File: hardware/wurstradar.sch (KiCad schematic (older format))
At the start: 11 parts

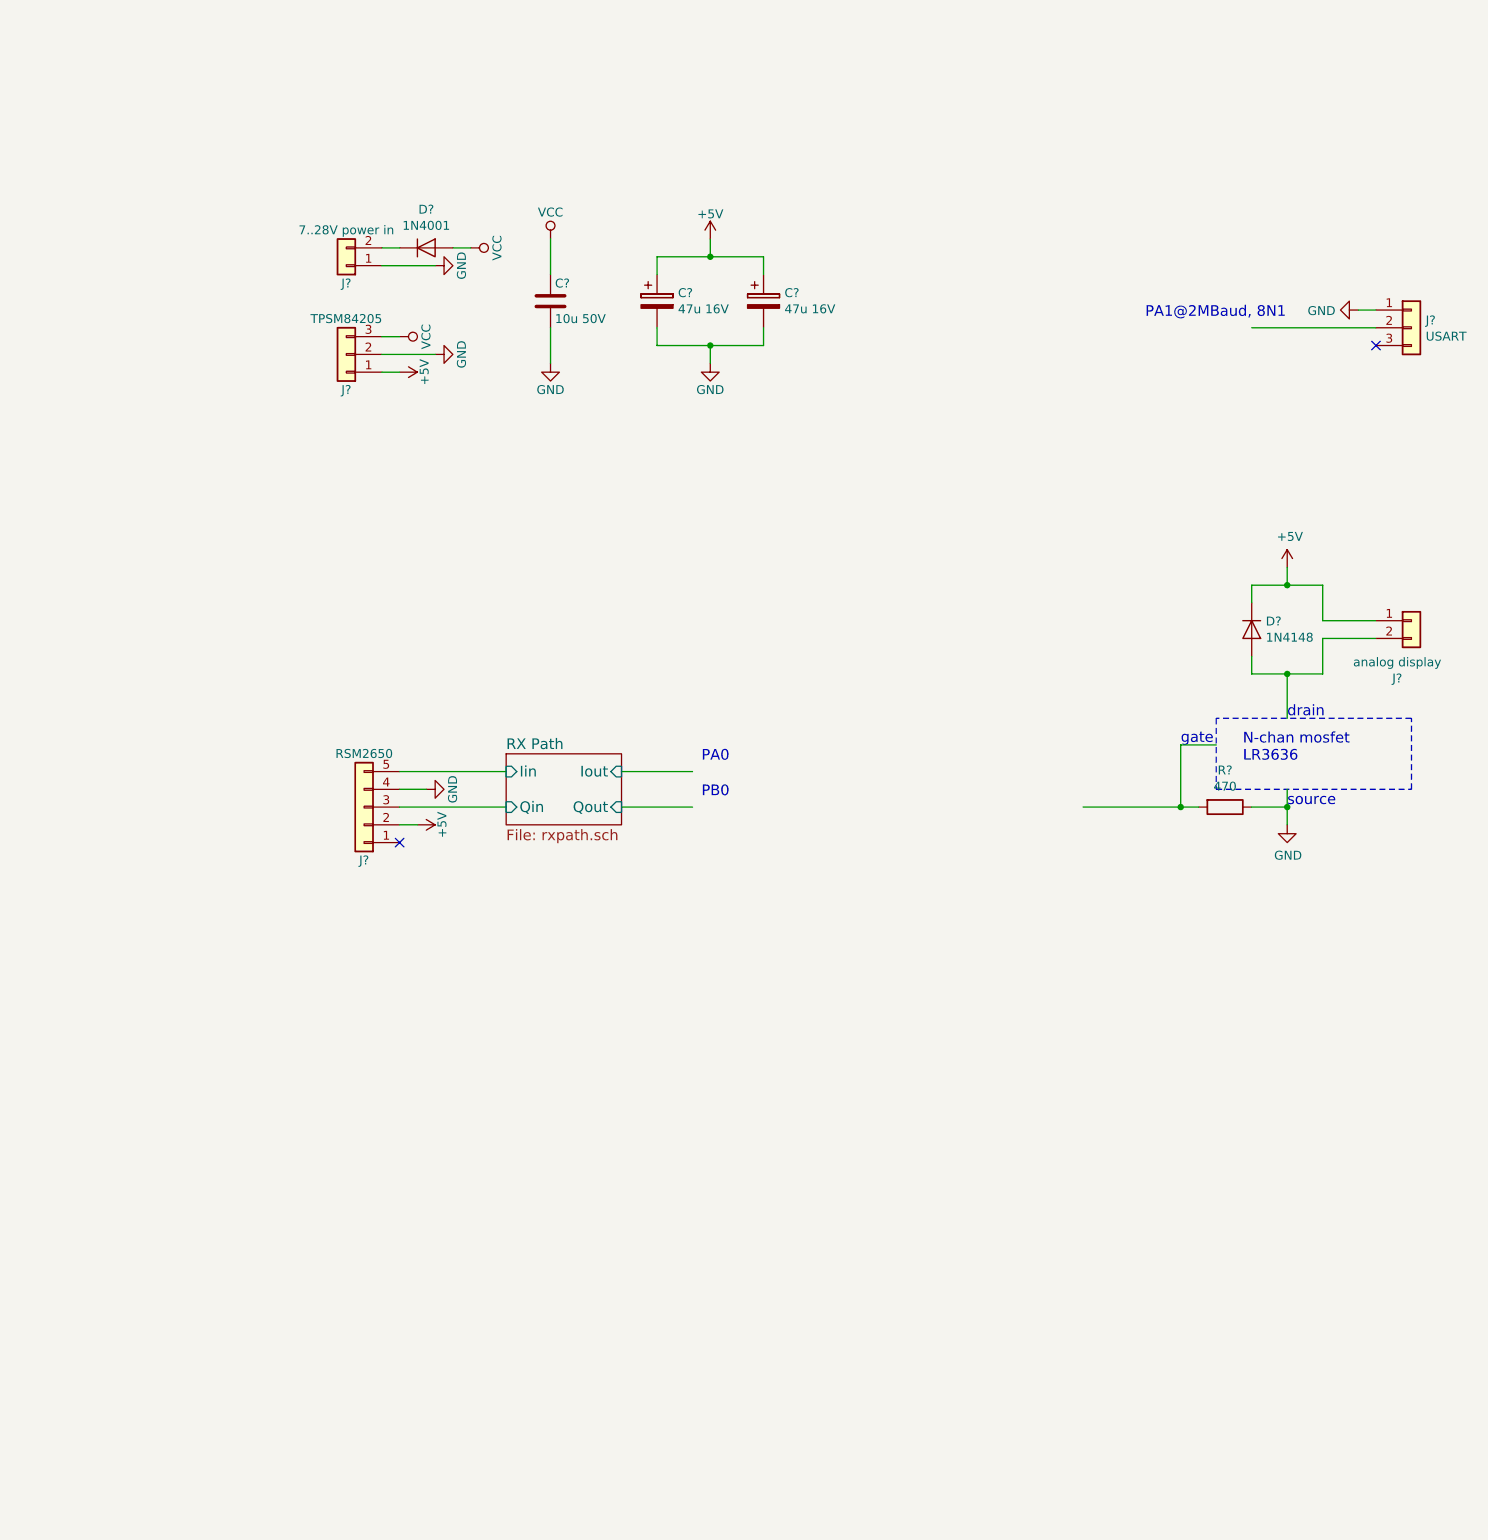
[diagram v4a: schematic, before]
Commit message: for long-term documentation: cleanup and port schematic to Kicad v5.1.4 and also export as PDF.
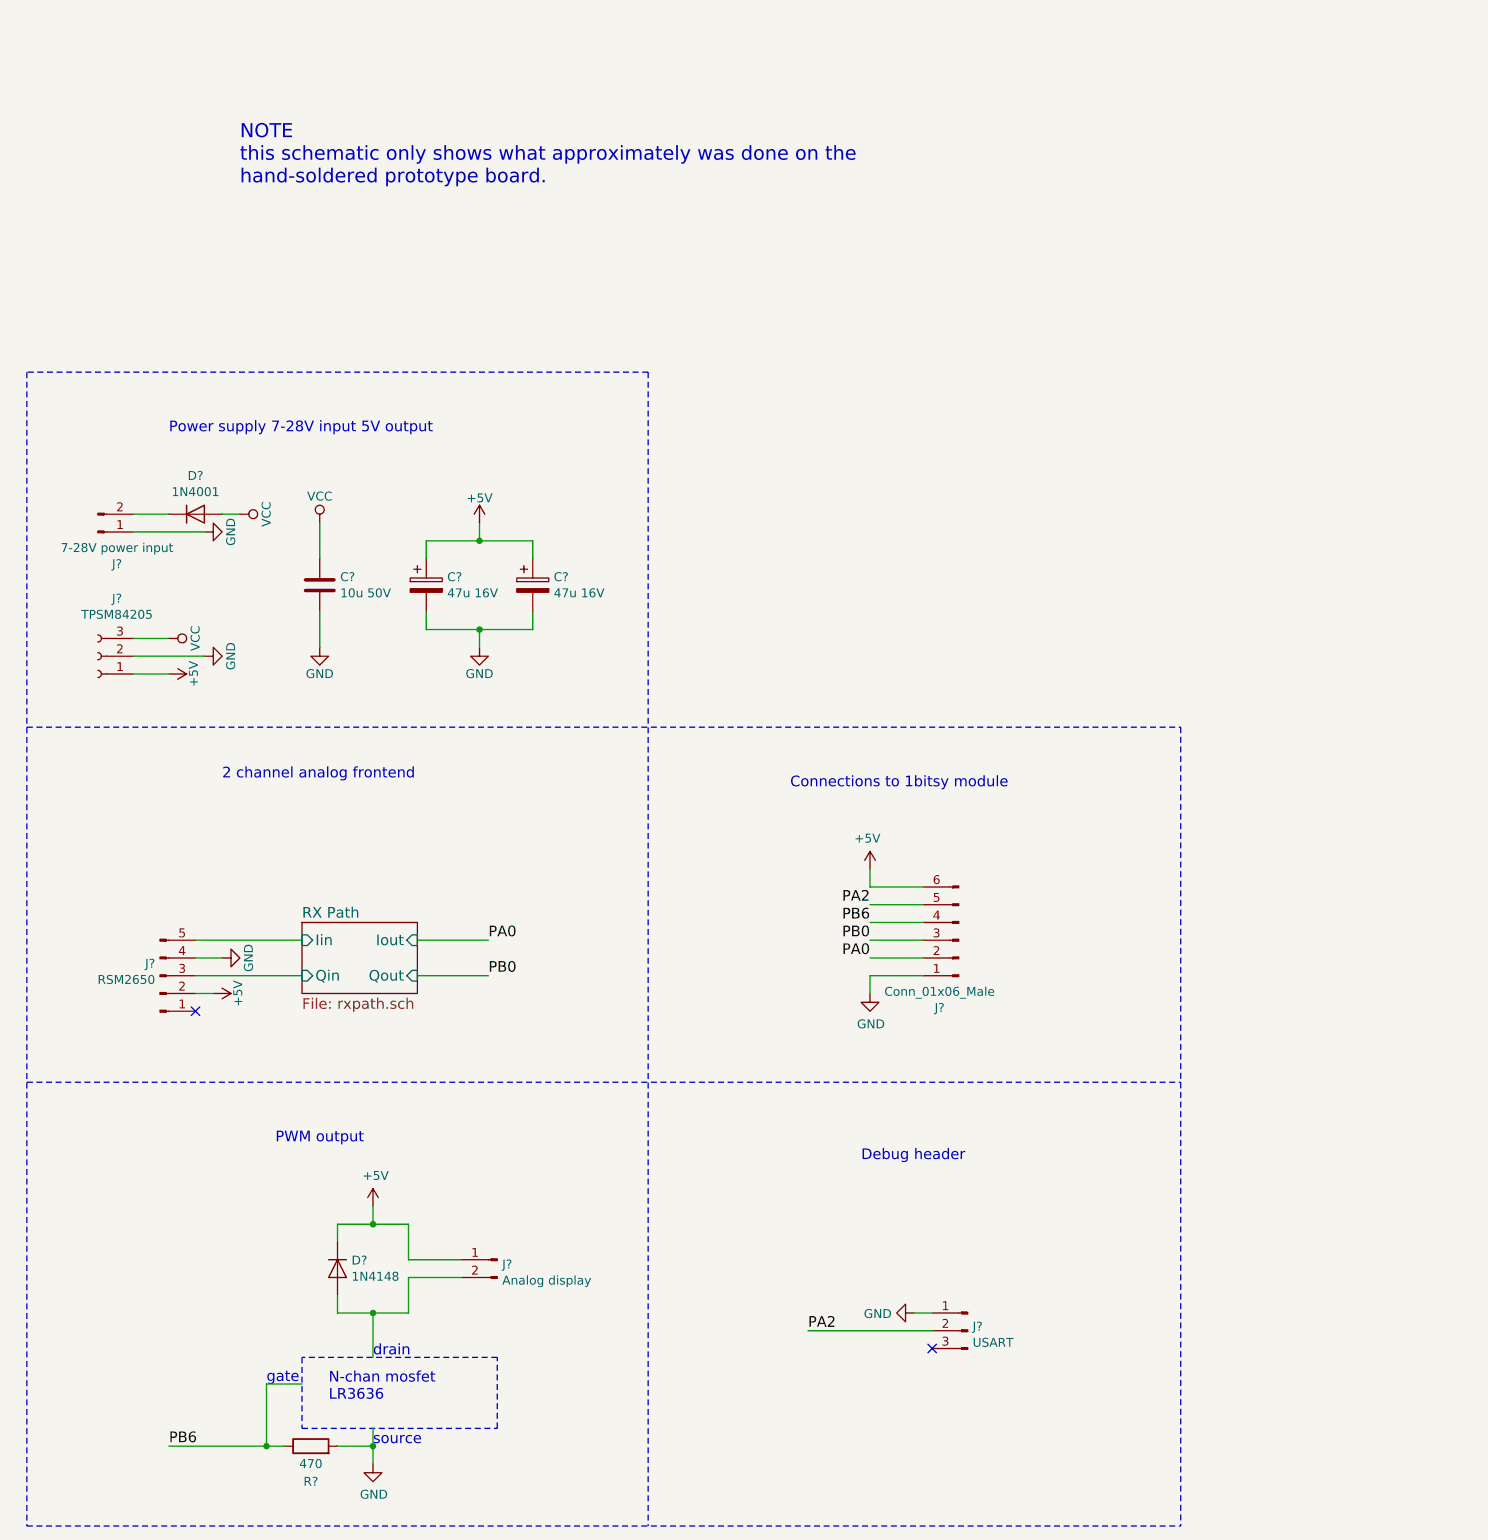
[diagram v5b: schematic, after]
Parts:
- removed C?: 10u 50V, symbol C
- removed C? (x2): 47u 16V, symbol CP
- removed D?: 1N4148, symbol D
- removed D?: 1N4001, symbol D
- removed J?: RSM2650, Pin_Headers:Pin_Header_Straight_1x05_Pitch2.54mm, symbol Conn_01x05
- removed J?: TPSM84205, symbol Conn_01x03
- removed J?: 7..28V power in, symbol Conn_01x02
- removed J?: USART, symbol Conn_01x03
- removed J?: analog display, symbol Conn_01x02
- removed R?: 470, symbol R
- added C?: 10u 50V, symbol Device:C
- added C? (x2): 47u 16V, symbol Device:CP
- added D?: 1N4148, symbol Device:D
- added D?: 1N4001, symbol Device:D
- added J?: 7-28V power input, symbol Connector:Conn_01x02_Male
- added J?: TPSM84205, symbol Connector:Conn_01x03_Female
- added J?: Conn_01x06_Male, symbol Connector:Conn_01x06_Male
- added J?: RSM2650, symbol Connector:Conn_01x05_Male
- added J?: Analog display, symbol Connector:Conn_01x02_Male
- added J?: USART, symbol Connector:Conn_01x03_Male
- added R?: 470, symbol Device:R
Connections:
- net labels added: PA0, PA2, PB0, PB6
- wire segments 39 -> 53
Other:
- note added: "2 channel analog frontend"
- note added: "Connections to 1bitsy module"
- note added: "Debug header"
- note added: "NOTE\nthis schematic only shows what approximately was done on the\nhand-soldered prototype board.\n"
- note added: "PWM output"
- note added: "Power supply 7-28V input 5V output"
- note removed: "PA0"
- note removed: "PA1@2MBaud, 8N1"
- note removed: "PB0"

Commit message: while at it, replace box-mosfet with a proper symbol
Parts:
- added M?: N-Channel MOSFET LR3636, symbol pspice:MNMOS
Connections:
- wire segments 53 -> 55
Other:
- note removed: "N-chan mosfet\nLR3636"
- note removed: "drain"
- note removed: "gate"
- note removed: "source"
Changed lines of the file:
@@
 Wire Wire Line
 	1800 9050 2350 9050
-Wire Wire Line
-	2350 9050 2350 8700
-Wire Wire Line
-	2350 8700 2550 8700
 Connection ~ 2350 9050
-Text Notes 2950 9050 0    60   ~ 0
-source
-Text Notes 2950 8550 0    60   ~ 0
-drain
-Text Notes 2350 8700 0    60   ~ 0
-gate
-Text Notes 2700 8800 0    60   ~ 0
-N-chan mosfet\nLR3636
-Wire Notes Line
-	2550 8550 2550 8950
-Wire Notes Line
-	2550 8950 3650 8950
-Wire Notes Line
-	3650 8950 3650 8550
-Wire Notes Line
-	3650 8550 2550 8550
 Wire Wire Line
 	1800 3800 1600 3800
@@
 	1    0    0    -1
 $EndComp
+Wire Wire Line
+	2350 9050 2350 8750
+Wire Wire Line
+	2350 8750 2650 8750
+$Comp
+L pspice:MNMOS M?
+U 1 1 5DED53BF
+P 2850 8750
+F 0 "M?" H 3138 8796 50  0000 L CNN
+F 1 "N-Channel MOSFET LR3636" H 3138 8705 50  0000 L CNN
+F 2 "" H 2825 8750 50  0001 C CNN
+F 3 "~" H 2825 8750 50  0001 C CNN
+	1    2850 8750
+	1    0    0    -1
+$EndComp
+Wire Wire Line
+	3050 8950 3050 9050
+Wire Wire Line
+	3050 9050 2950 9050
 $EndSCHEMATC
